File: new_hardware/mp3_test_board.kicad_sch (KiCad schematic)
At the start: 0 parts

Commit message: some fucking changes
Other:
- added sheet WI-FI (WI-FI.kicad_sch)
- sheet SOC ports: added AUDIO_PWR_EN, WIFI_SDIO_CLK, WIFI_SDIO_CMD, WIFI_SDIO_D0, WIFI_SDIO_D1, WIFI_SDIO_D2, WIFI_SDIO_D3; removed none

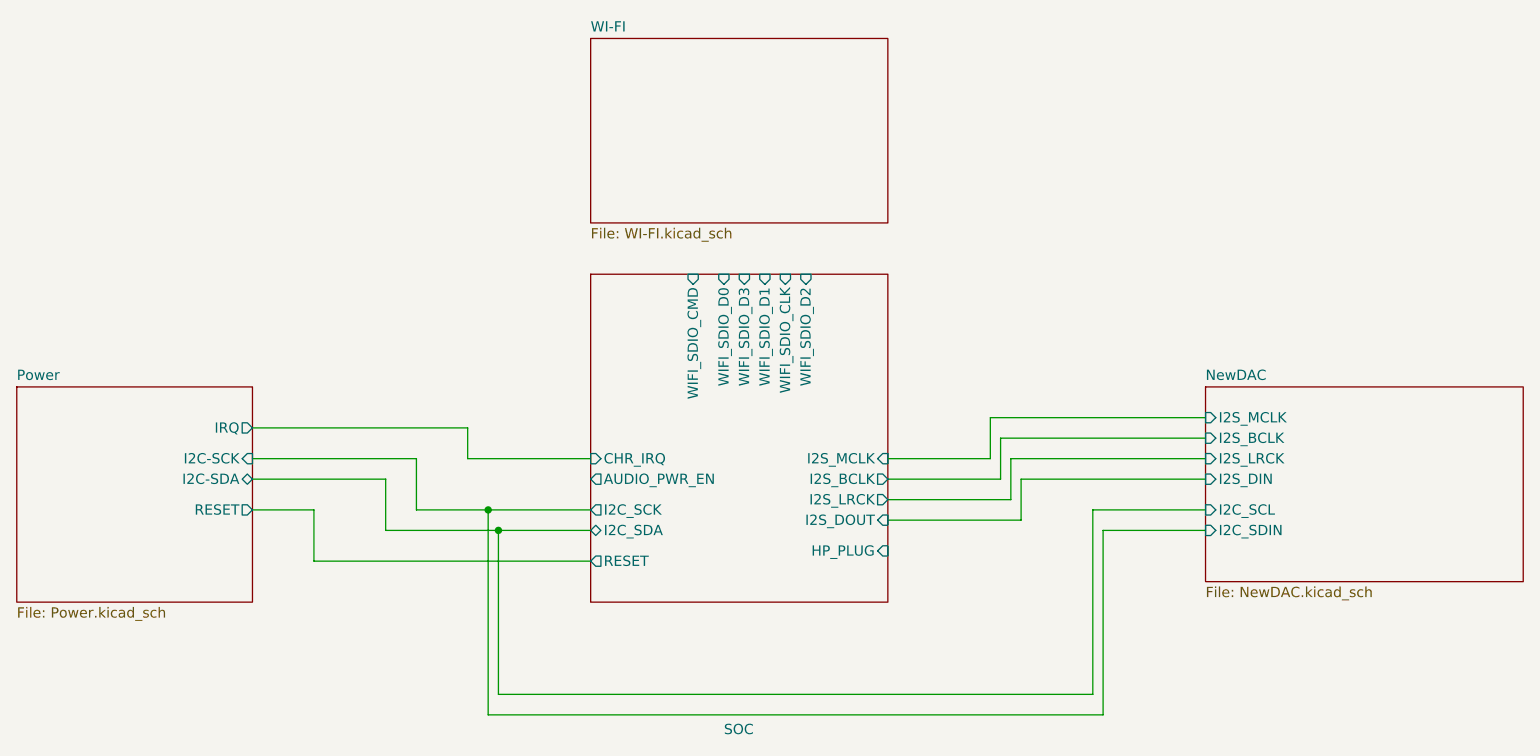
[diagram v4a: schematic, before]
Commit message: device tree is changed
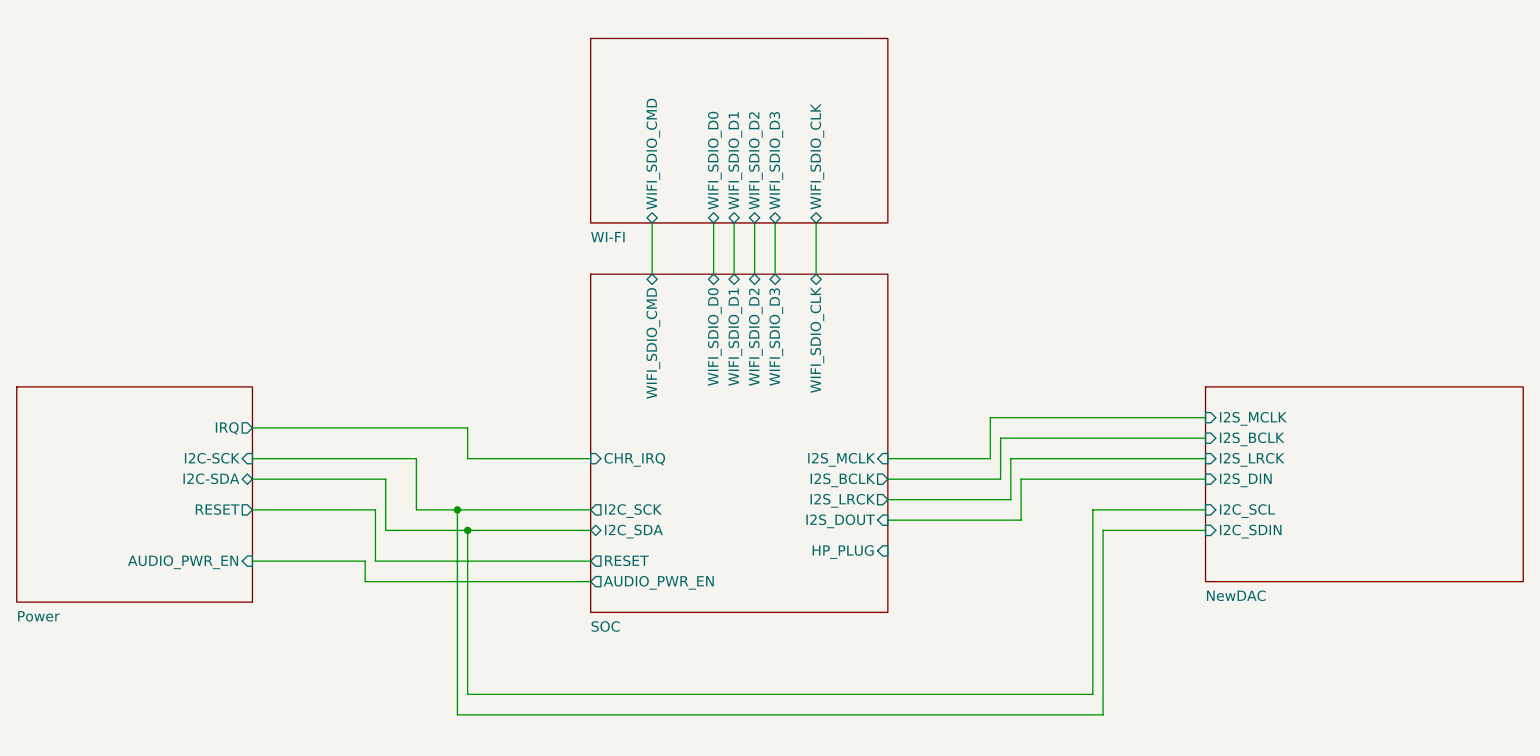
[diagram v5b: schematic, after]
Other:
- sheet Power ports: added AUDIO_PWR_EN; removed none
- sheet WI-FI ports: added WIFI_SDIO_CLK, WIFI_SDIO_CMD, WIFI_SDIO_D0, WIFI_SDIO_D1, WIFI_SDIO_D2, WIFI_SDIO_D3; removed none

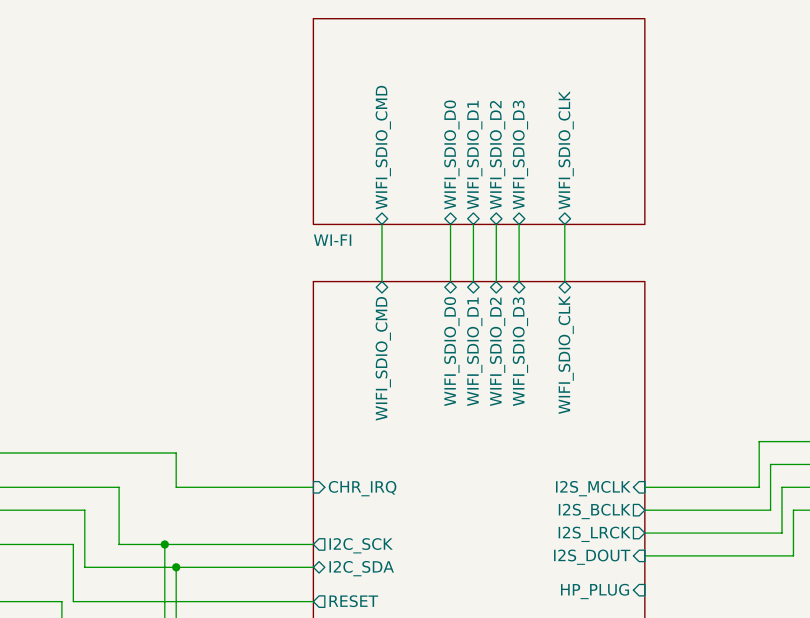
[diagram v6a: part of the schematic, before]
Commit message: wi-fi module is moved to closer board outline,unused files are removed
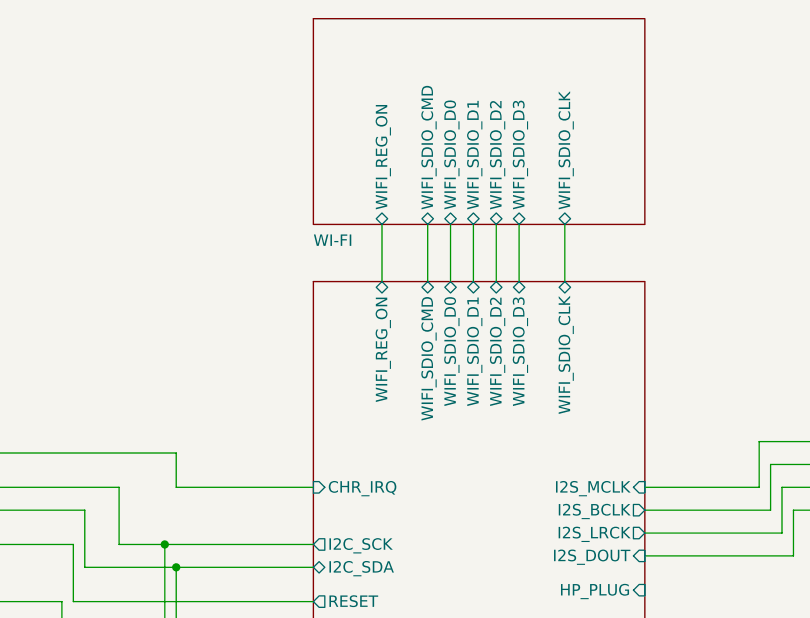
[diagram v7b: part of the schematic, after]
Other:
- sheet SOC ports: added WIFI_REG_ON; removed none
- sheet WI-FI ports: added WIFI_REG_ON; removed none
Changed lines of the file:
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@@
   (junction (at 107.95 87.63) (diameter 0) (color 0 0 0 0)
   )
+  (wire (pts (xy 130.81 49.53) (xy 130.81 55.88))
+    (stroke (width 0) (type default) (color 0 0 0 0))
+  )
   (wire (pts (xy 81.28 91.44) (xy 95.25 91.44))
     (stroke (width 0) (type default) (color 0 0 0 0))
@@
     (stroke (width 0) (type default) (color 0 0 0 0))
   )
-  (wire (pts (xy 130.81 49.53) (xy 130.81 55.88))
+  (wire (pts (xy 135.89 49.53) (xy 135.89 55.88))
     (stroke (width 0) (type default) (color 0 0 0 0))
   )
@@
       (effects (font (size 1.27 1.27)) (justify left))
     )
-    (pin "WIFI_SDIO_CMD" bidirectional (at 130.81 55.88 90)
+    (pin "WIFI_SDIO_CMD" bidirectional (at 135.89 55.88 90)
       (effects (font (size 1.27 1.27)) (justify right))
     )
@@
     )
     (pin "WIFI_SDIO_D1" bidirectional (at 140.97 55.88 90)
+      (effects (font (size 1.27 1.27)) (justify right))
+    )
+    (pin "WIFI_REG_ON" bidirectional (at 130.81 55.88 90)
       (effects (font (size 1.27 1.27)) (justify right))
     )
@@
       (effects (font (size 1.27 1.27)) (justify left))
     )
-    (pin "WIFI_SDIO_CMD" bidirectional (at 130.81 49.53 270)
+    (pin "WIFI_SDIO_CMD" bidirectional (at 135.89 49.53 270)
       (effects (font (size 1.27 1.27)) (justify left))
     )
@@
     )
     (pin "WIFI_SDIO_D3" bidirectional (at 146.05 49.53 270)
+      (effects (font (size 1.27 1.27)) (justify left))
+    )
+    (pin "WIFI_REG_ON" bidirectional (at 130.81 49.53 270)
       (effects (font (size 1.27 1.27)) (justify left))
     )
@@
       (reference "#PWR030") (unit 1) (value "GND") (footprint "")
     )
+    (path "/aa3ce668-54ef-4a1c-908c-ffe0f988f256/5145b50a-dd7c-4bef-800e-7866dda6b6b2"
+      (reference "#PWR031") (unit 1) (value "GND") (footprint "")
+    )
     (path "/494fd4b1-1de7-49fe-827f-914491efe850/c8b4dc99-62f8-40b8-939a-136c545bcb51"
       (reference "#PWR032") (unit 1) (value "GND") (footprint "")
@@
       (reference "#PWR033") (unit 1) (value "GND") (footprint "")
     )
+    (path "/aa3ce668-54ef-4a1c-908c-ffe0f988f256/d5da21dc-c508-464b-ad08-aafa84559b5b"
+      (reference "#PWR034") (unit 1) (value "GND") (footprint "")
+    )
+    (path "/aa3ce668-54ef-4a1c-908c-ffe0f988f256/b95f9795-080f-4599-8456-17525e8ad7dd"
+      (reference "#PWR035") (unit 1) (value "GND") (footprint "")
+    )
     (path "/494fd4b1-1de7-49fe-827f-914491efe850/a0744d59-4ee1-4d0e-afc4-b289ed151b0c"
       (reference "#PWR036") (unit 1) (value "GND") (footprint "")
@@
       (reference "#PWR042") (unit 1) (value "+3V3") (footprint "")
     )
+    (path "/aa3ce668-54ef-4a1c-908c-ffe0f988f256/08962e15-4224-4401-bcbf-d29d78eddeb8"
+      (reference "#PWR043") (unit 1) (value "GND") (footprint "")
+    )
     (path "/494fd4b1-1de7-49fe-827f-914491efe850/fa89a5a2-7f85-48bb-a4c8-4c8c8b5ba6b8"
       (reference "#PWR044") (unit 1) (value "+3V3") (footprint "")
@@
       (reference "#PWR0145") (unit 1) (value "+3V3") (footprint "")
     )
-    (path "/aa3ce668-54ef-4a1c-908c-ffe0f988f256/5145b50a-dd7c-4bef-800e-7866dda6b6b2"
-      (reference "#PWR?") (unit 1) (value "GND") (footprint "")
-    )
     (path "/494fd4b1-1de7-49fe-827f-914491efe850/e968bfe4-ae20-4952-9243-0ed30127e608"
       (reference "C1") (unit 1) (value "100n") (footprint "rlib_passive:C_0603_1608Metric")
@@
       (reference "C75") (unit 1) (value "10u") (footprint "rlib_passive:C_0603_1608Metric")
     )
+    (path "/aa3ce668-54ef-4a1c-908c-ffe0f988f256/de966aa7-aa92-4844-b179-17a3eaa326c3"
+      (reference "C76") (unit 1) (value "18p") (footprint "rlib_passive:C_0603_1608Metric")
+    )
+    (path "/aa3ce668-54ef-4a1c-908c-ffe0f988f256/d5f28431-92af-44ac-8a69-35e71f4437d8"
+      (reference "C77") (unit 1) (value "18p") (footprint "rlib_passive:C_0603_1608Metric")
+    )
     (path "/494fd4b1-1de7-49fe-827f-914491efe850/c7d3782f-411c-4636-8559-fbb9d4580864"
       (reference "D1") (unit 1) (value "PESD3V3L1BA") (footprint "rlib_passive:D_SOD-323F")
@@
     )
     (path "/aa3ce668-54ef-4a1c-908c-ffe0f988f256/2f8622ce-2d00-43ac-9250-5e439ea80ed6"
-      (reference "RF?") (unit 1) (value "BWIPX-1-001E") (footprint "rlib_connectors:IPEX-SMD_BWIPX-1-001E")
+      (reference "RF1") (unit 1) (value "BWIPX-1-001E") (footprint "rlib_connectors:IPEX-SMD_BWIPX-1-001E")
     )
     (path "/494fd4b1-1de7-49fe-827f-914491efe850/1056e97f-1b11-45e8-af12-b3d441c2b63a"
@@
       (reference "TP23") (unit 1) (value "TestPoint") (footprint "TestPoint:TestPoint_Pad_D1.0mm")
     )
+    (path "/884771b3-a958-42f5-9d43-01d94fb8bdd5/dc65fb21-af5c-4f12-b68e-49b3c1469cee"
+      (reference "TP24") (unit 1) (value "TestPoint") (footprint "TestPoint:TestPoint_Pad_D1.0mm")
+    )
+    (path "/884771b3-a958-42f5-9d43-01d94fb8bdd5/d881ad36-8e04-4b9c-b3ab-72d6a46cb9d0"
+      (reference "TP25") (unit 1) (value "TestPoint") (footprint "TestPoint:TestPoint_Pad_D1.0mm")
+    )
     (path "/494fd4b1-1de7-49fe-827f-914491efe850/13de2545-793e-4bc2-aed9-627dbd3bee7d"
       (reference "U1") (unit 1) (value "F133") (footprint "rlib_ic:LQFP-128_14x14mm_P0.4mm")
@@
       (reference "Y1") (unit 1) (value "12.88727") (footprint "rlib_passive:12.88727")
     )
-  )
+    (path "/aa3ce668-54ef-4a1c-908c-ffe0f988f256/441f5945-14dc-494e-bafe-7c2652c02e34"
+      (reference "Y2") (unit 1) (value "26МHz") (footprint "rlib_passive:CRYSTAL-SMD_4P-L1.6-W1.2-BL")
+    )
+  )
